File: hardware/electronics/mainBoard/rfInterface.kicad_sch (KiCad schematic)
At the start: 0 parts

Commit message: added rf interface sch
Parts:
- added AE1: TNC, symbol lib_sch:Antenna_Shield
- added AE3, AE4: SMA, symbol lib_sch:Antenna_Shield
- added C85, C86: 100nF, symbol lib_sch:C
- added C87: 9.1pF, symbol lib_sch:C
- added C88: 5.6pF, symbol lib_sch:C_horizontal
- added C89: 9.1pF, symbol lib_sch:C_horizontal
- added C90: 100pF, symbol lib_sch:C_horizontal
- added C91: 100pF, symbol lib_sch:C
- added J12, J13, J14, J15: CONMHF1-SMD-T, symbol lib_sch:Conn_Coaxial
- added L4: 15nH, symbol lib_sch:L
- added L5: 6.8nH, symbol lib_sch:L
- added R57: 750R, symbol lib_sch:R
- added R58: 267R, symbol lib_sch:R_horizontal
- added R59: 49R9, symbol lib_sch:R
- added U17: PMA2-162LNA+, symbol lib_sch:PMA2-162LNA+
- added U18: QCN-19D+, symbol lib_sch:QCN-19D+
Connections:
- new net: C88.2, R58.1
- new net AUX_RF-IN: AE3.1 (A), J15.1 (In)
- new net GNSS_CONN1: J12.1 (In), U18.4 (PORT1)
- new net GNSS_CONN2: J13.1 (In), U18.6 (PORT2)
- new net GNSS_RF-IN: AE1.1 (A), C89.1
- new net LNA_BIAS: R57.2, U17.4 (BIAS)
- new net LNA_FB: C88.1, U17.5 (FB)
- new net LNA_RBIAS: C85.1, C86.1, C87.1, L4.1, R57.1
- new net LNA_RF-GND: C91.1, L5.2, U17.3 (RF-GND)
- new net LNA_RF-IN: C89.2, L5.1, U17.2 (RF-IN)
- new net LNA_RF-OUT: C90.1, L4.2, R58.2, U17.7 (RF-OUT)
- new net LTE_RF-IN: AE4.1 (A), J14.1 (In)
- new net RF-SPLIT_50R: R59.1, U18.3 (50R)
- new net RF-SPLIT_SUM: C90.2, U18.1 (SUM)
- new net VSS: AE1.2 (Shield), AE3.2 (Shield), AE4.2 (Shield), C85.2, C86.2, C87.2, C91.2, J12.2 (Ext), J13.2 (Ext), J14.2 (Ext), J15.2 (Ext), R59.2, U17.1 (NC), U17.6 (NC), U17.8 (GND), U17.9 (GND), U18.2 (GND), U18.5 (GND)
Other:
- note added: "AUX Card Cable"
- note added: "GNSS Card Cable"
- note added: "LTE Card Cable"

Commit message: fixed power flags
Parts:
- AE3: now not fitted
- renumbered AE4 to AE2, C85 to C71, C86 to C72, C87 to C73, C88 to C74, C89 to C75, C90 to C76, C91 to C77, R57 to R48, R58 to R49, R59 to R50, U17 to U16, U18 to U17

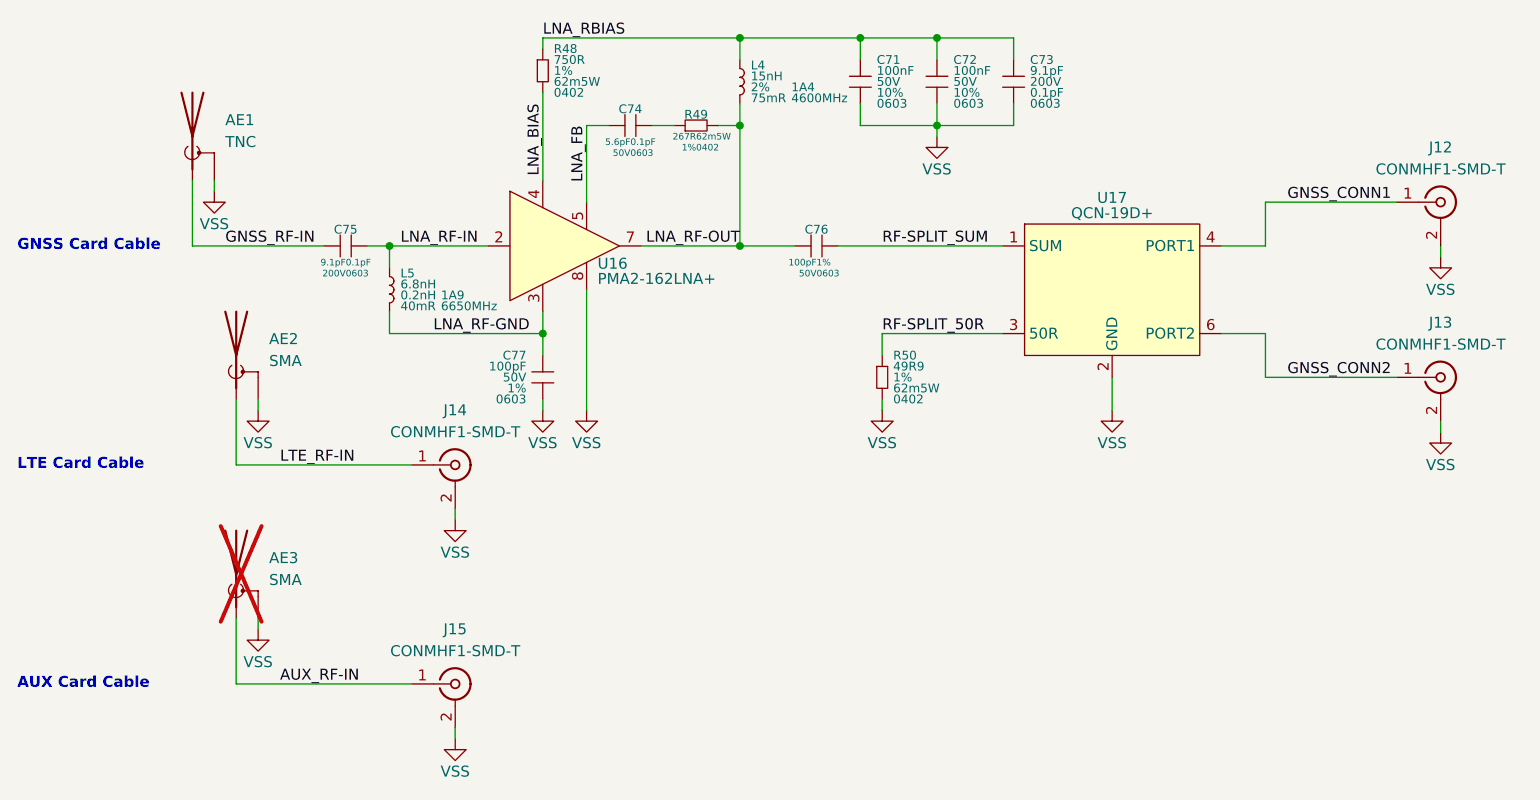
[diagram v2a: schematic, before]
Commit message: updated capacitors
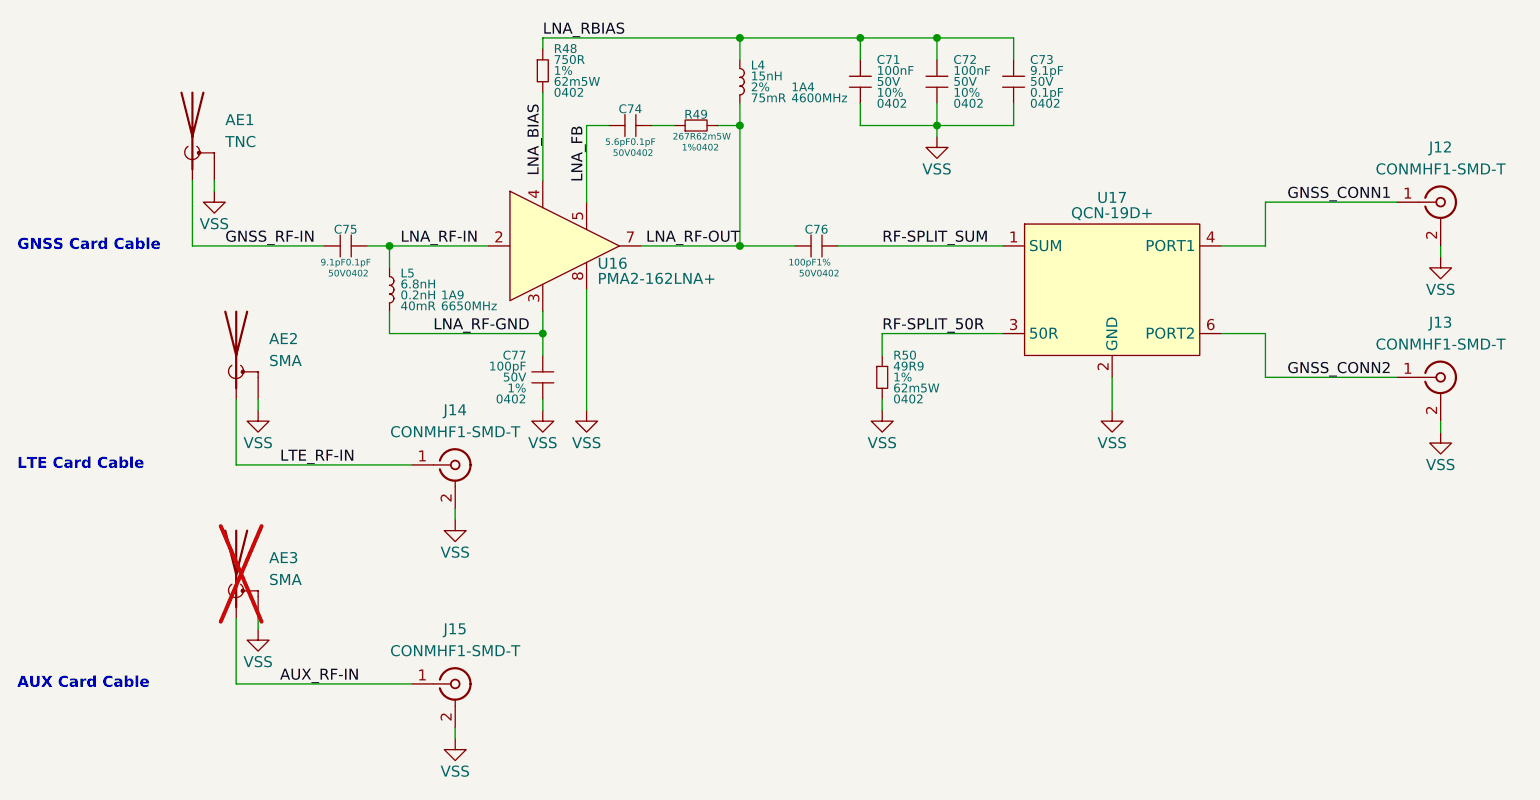
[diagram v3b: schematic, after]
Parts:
- C71, C72: DKPN 478-KAM15AR71H104KTCT-ND -> 490-GRT155R71H104KE01DCT-ND; MPN 06035C104K4T2A -> GRT155R71H104KE01D; Manufacturer KYOCERA AVX -> Murata Electronics; Package 0603 -> 0402
- C73, C75: DKPN 478-KGQ15ACG2D9R1BTCT-ND -> 490-GCM1555C1H9R1BA16DCT-ND; MPN KGQ15ACG2D9R1BT -> GCM1555C1H9R1BA16D; Manufacturer KYOCERA AVX -> Murata Electronics; Package 0603 -> 0402; Voltage Rating 200V -> 50V
- C74: DKPN 478-KGQ15ACG1H5R6BTCT-ND -> 490-14424-1-ND; MPN KGQ15ACG1H5R6BT -> GCM1555C1H5R6BA16D; Manufacturer KYOCERA AVX -> Murata Electronics; Package 0603 -> 0402
- C76, C77: DKPN 478-KGQ15ACG1H101FTCT-ND -> 490-14349-1-ND; MPN KGQ15ACG1H101FT -> GCM1555C1H101FA16D; Manufacturer KYOCERA AVX -> Murata Electronics; Package 0603 -> 0402

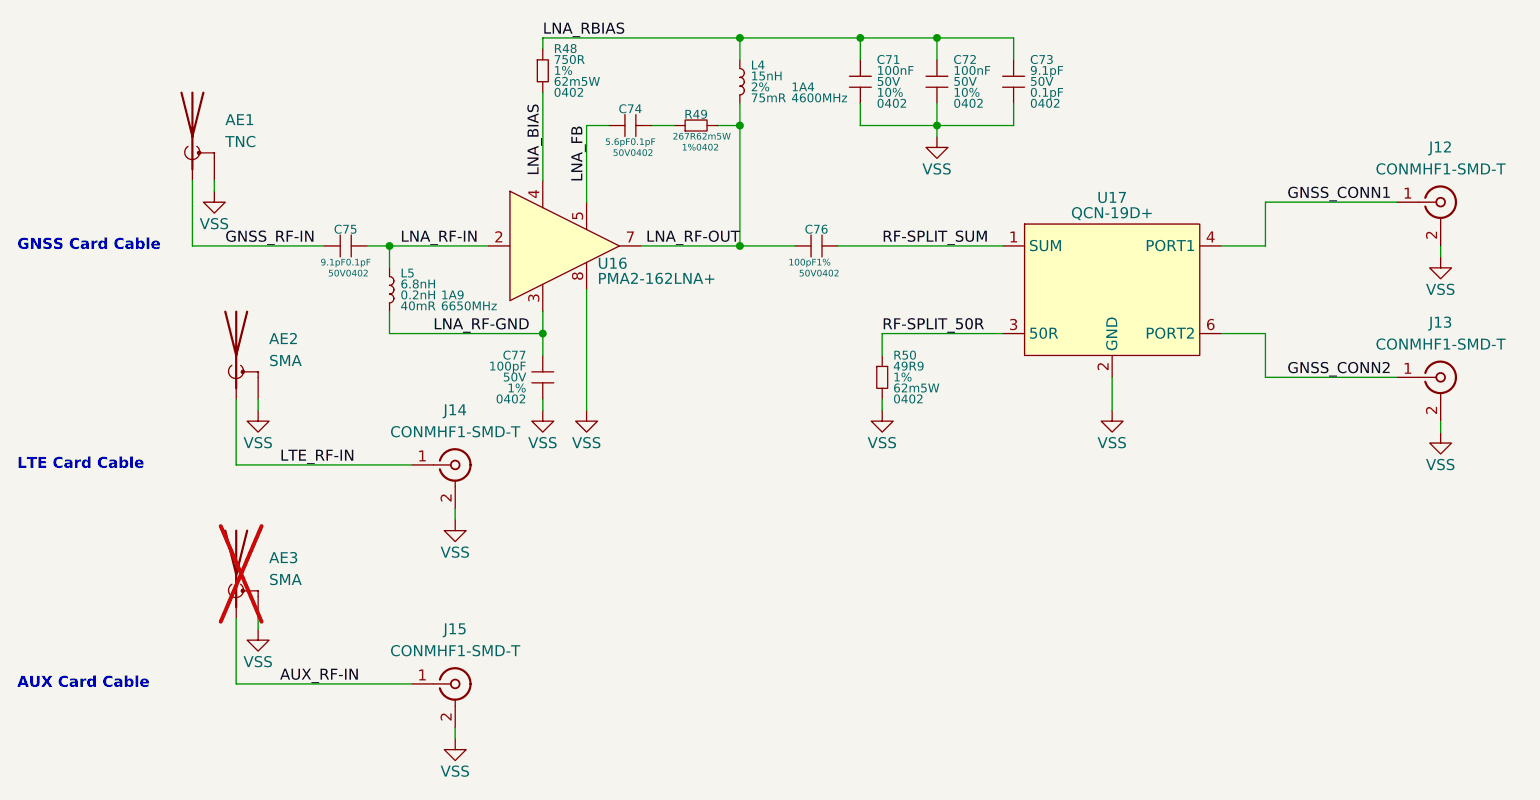
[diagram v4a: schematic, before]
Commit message: updated symbol refs
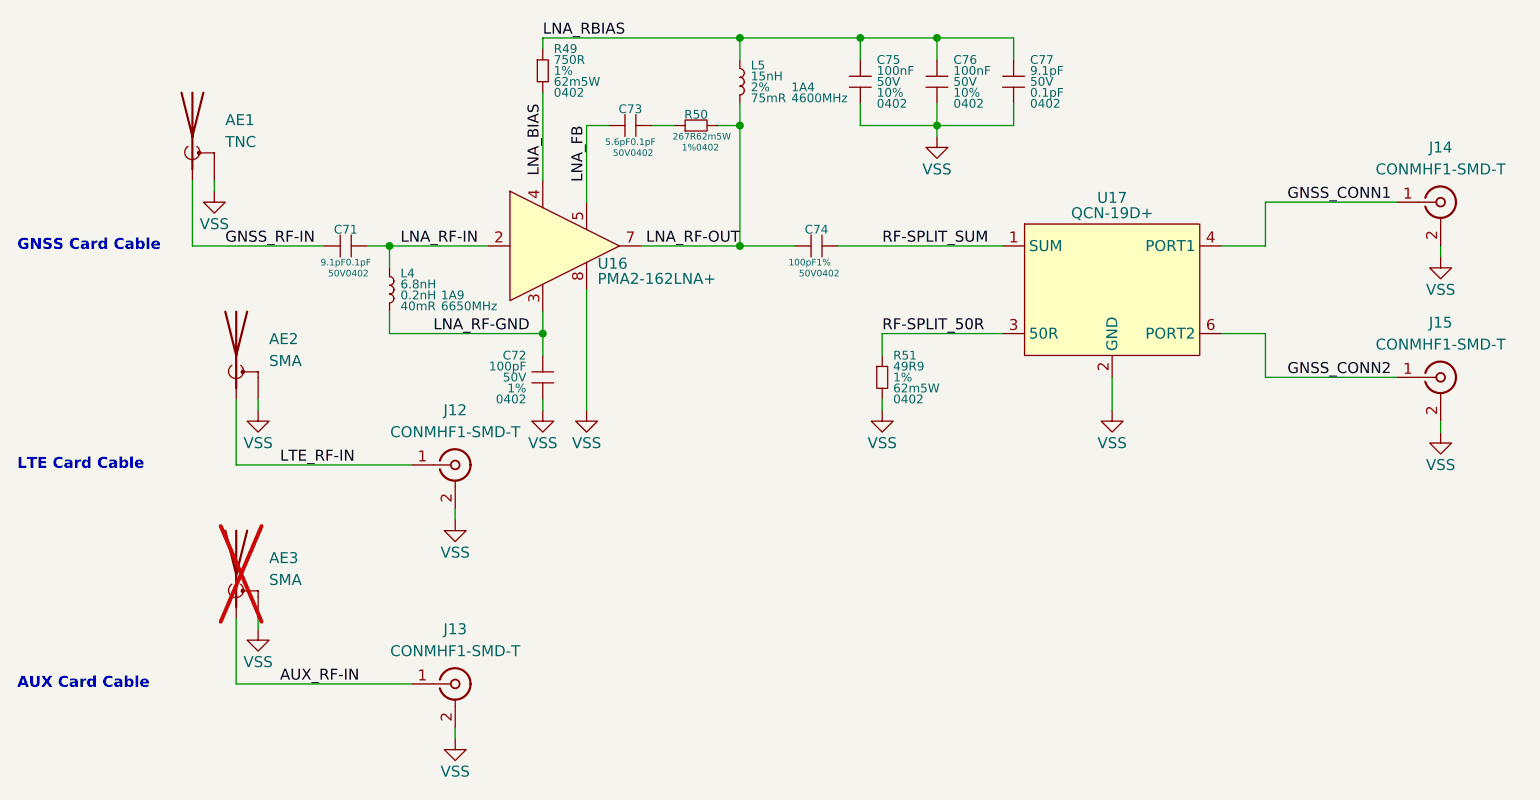
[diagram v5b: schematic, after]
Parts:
- renumbered C75 to C71, C77 to C72, C74 to C73, C76 to C74, C71 to C75, C72 to C76, C73 to C77, J14 to J12, J15 to J13, J12 to J14, J13 to J15, L5 to L4, L4 to L5, R48 to R49, R49 to R50, R50 to R51
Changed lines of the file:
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@@
 		(dnp no)
 		(fields_autoplaced yes)
-		(property "Reference" "#PWR0178"
+		(property "Reference" "#PWR0172"
 			(at 114.3 133.35 0)
 			(effects
@@
 			(project "mainBoard"
 				(path "/be16e32f-2ccf-4272-9ec7-94d5fe7a55e0/9566ea48-a930-4cf1-864c-3e42d00ab717"
-					(reference "#PWR0178")
+					(reference "#PWR0172")
 					(unit 1)
 				)
@@
 		(dnp no)
 		(fields_autoplaced yes)
-		(property "Reference" "C76"
+		(property "Reference" "C74"
 			(at 156.21 74.295 0)
 			(do_not_autoplace yes)
@@
 			(project "mainBoard"
 				(path "/be16e32f-2ccf-4272-9ec7-94d5fe7a55e0/9566ea48-a930-4cf1-864c-3e42d00ab717"
-					(reference "C76")
+					(reference "C74")
 					(unit 1)
 				)
@@
 		(dnp no)
 		(fields_autoplaced yes)
-		(property "Reference" "R49"
+		(property "Reference" "R50"
 			(at 142.24 60.96 0)
 			(do_not_autoplace yes)
@@
 			(project ""
 				(path "/be16e32f-2ccf-4272-9ec7-94d5fe7a55e0/9566ea48-a930-4cf1-864c-3e42d00ab717"
-					(reference "R49")
+					(reference "R50")
 					(unit 1)
 				)
@@
 		(dnp no)
 		(fields_autoplaced yes)
-		(property "Reference" "#PWR0175"
+		(property "Reference" "#PWR0179"
 			(at 228.6 97.79 0)
 			(effects
@@
 			(project "mainBoard"
 				(path "/be16e32f-2ccf-4272-9ec7-94d5fe7a55e0/9566ea48-a930-4cf1-864c-3e42d00ab717"
-					(reference "#PWR0175")
+					(reference "#PWR0179")
 					(unit 1)
 				)
@@
 		(dnp no)
 		(fields_autoplaced yes)
-		(property "Reference" "#PWR0176"
+		(property "Reference" "#PWR0171"
 			(at 114.3 107.95 0)
 			(effects
@@
 			(project "mainBoard"
 				(path "/be16e32f-2ccf-4272-9ec7-94d5fe7a55e0/9566ea48-a930-4cf1-864c-3e42d00ab717"
-					(reference "#PWR0176")
+					(reference "#PWR0171")
 					(unit 1)
 				)
@@
 		(on_board yes)
 		(dnp no)
-		(property "Reference" "L5"
+		(property "Reference" "L4"
 			(at 107.95 79.375 0)
 			(do_not_autoplace yes)
@@
 			(project ""
 				(path "/be16e32f-2ccf-4272-9ec7-94d5fe7a55e0/9566ea48-a930-4cf1-864c-3e42d00ab717"
-					(reference "L5")
+					(reference "L4")
 					(unit 1)
 				)
@@
 		(dnp no)
 		(fields_autoplaced yes)
-		(property "Reference" "#PWR0177"
+		(property "Reference" "#PWR0170"
 			(at 91.44 120.65 0)
 			(effects
@@
 			(project "mainBoard"
 				(path "/be16e32f-2ccf-4272-9ec7-94d5fe7a55e0/9566ea48-a930-4cf1-864c-3e42d00ab717"
-					(reference "#PWR0177")
+					(reference "#PWR0170")
 					(unit 1)
 				)
@@
 		(on_board yes)
 		(dnp no)
-		(property "Reference" "J15"
+		(property "Reference" "J13"
 			(at 114.3 120.65 0)
 			(effects
@@
 			(project "mainBoard"
 				(path "/be16e32f-2ccf-4272-9ec7-94d5fe7a55e0/9566ea48-a930-4cf1-864c-3e42d00ab717"
-					(reference "J15")
+					(reference "J13")
 					(unit 1)
 				)
@@
 		(on_board yes)
 		(dnp no)
-		(property "Reference" "J12"
+		(property "Reference" "J14"
 			(at 228.6 64.77 0)
 			(effects
@@
 			(project ""
 				(path "/be16e32f-2ccf-4272-9ec7-94d5fe7a55e0/9566ea48-a930-4cf1-864c-3e42d00ab717"
-					(reference "J12")
+					(reference "J14")
 					(unit 1)
 				)
@@
 		(dnp no)
 		(fields_autoplaced yes)
-		(property "Reference" "#PWR0170"
+		(property "Reference" "#PWR0169"
 			(at 91.44 95.25 0)
 			(effects
@@
 			(project "mainBoard"
 				(path "/be16e32f-2ccf-4272-9ec7-94d5fe7a55e0/9566ea48-a930-4cf1-864c-3e42d00ab717"
-					(reference "#PWR0170")
+					(reference "#PWR0169")
 					(unit 1)
 				)
@@
 		(dnp no)
 		(fields_autoplaced yes)
-		(property "Reference" "R48"
+		(property "Reference" "R49"
 			(at 125.73 53.34 0)
 			(do_not_autoplace yes)
@@
 			(project ""
 				(path "/be16e32f-2ccf-4272-9ec7-94d5fe7a55e0/9566ea48-a930-4cf1-864c-3e42d00ab717"
-					(reference "R48")
+					(reference "R49")
 					(unit 1)
 				)
@@
 		(dnp no)
 		(fields_autoplaced yes)
-		(property "Reference" "C71"
+		(property "Reference" "C75"
 			(at 163.195 54.61 0)
 			(do_not_autoplace yes)
@@
 			(project "mainBoard"
 				(path "/be16e32f-2ccf-4272-9ec7-94d5fe7a55e0/9566ea48-a930-4cf1-864c-3e42d00ab717"
-					(reference "C71")
+					(reference "C75")
 					(unit 1)
 				)
@@
 		(on_board yes)
 		(dnp no)
-		(property "Reference" "J13"
+		(property "Reference" "J15"
 			(at 228.6 85.09 0)
 			(effects
@@
 			(project "mainBoard"
 				(path "/be16e32f-2ccf-4272-9ec7-94d5fe7a55e0/9566ea48-a930-4cf1-864c-3e42d00ab717"
-					(reference "J13")
+					(reference "J15")
 					(unit 1)
 				)
@@
 		(on_board yes)
 		(dnp no)
-		(property "Reference" "L4"
+		(property "Reference" "L5"
 			(at 148.59 55.245 0)
 			(do_not_autoplace yes)
@@
 			(project "mainBoard"
 				(path "/be16e32f-2ccf-4272-9ec7-94d5fe7a55e0/9566ea48-a930-4cf1-864c-3e42d00ab717"
-					(reference "L4")
+					(reference "L5")
 					(unit 1)
 				)
@@
 		(dnp no)
 		(fields_autoplaced yes)
-		(property "Reference" "#PWR0173"
+		(property "Reference" "#PWR0175"
 			(at 163.83 95.25 0)
 			(effects
@@
 			(project "mainBoard"
 				(path "/be16e32f-2ccf-4272-9ec7-94d5fe7a55e0/9566ea48-a930-4cf1-864c-3e42d00ab717"
-					(reference "#PWR0173")
+					(reference "#PWR0175")
 					(unit 1)
 				)
@@
 		(dnp no)
 		(fields_autoplaced yes)
-		(property "Reference" "R50"
+		(property "Reference" "R51"
 			(at 165.1 88.9 0)
 			(do_not_autoplace yes)
@@
 			(project "mainBoard"
 				(path "/be16e32f-2ccf-4272-9ec7-94d5fe7a55e0/9566ea48-a930-4cf1-864c-3e42d00ab717"
-					(reference "R50")
+					(reference "R51")
 					(unit 1)
 				)
@@
 		(dnp no)
 		(fields_autoplaced yes)
-		(property "Reference" "#PWR0169"
+		(property "Reference" "#PWR0178"
 			(at 228.6 77.47 0)
 			(effects
@@
 			(project "mainBoard"
 				(path "/be16e32f-2ccf-4272-9ec7-94d5fe7a55e0/9566ea48-a930-4cf1-864c-3e42d00ab717"
-					(reference "#PWR0169")
+					(reference "#PWR0178")
 					(unit 1)
 				)
@@
 		(dnp no)
 		(fields_autoplaced yes)
-		(property "Reference" "#PWR0167"
+		(property "Reference" "#PWR0176"
 			(at 170.18 63.5 0)
 			(effects
@@
 			(project "mainBoard"
 				(path "/be16e32f-2ccf-4272-9ec7-94d5fe7a55e0/9566ea48-a930-4cf1-864c-3e42d00ab717"
-					(reference "#PWR0167")
+					(reference "#PWR0176")
 					(unit 1)
 				)
@@
 		(dnp no)
 		(fields_autoplaced yes)
-		(property "Reference" "C72"
+		(property "Reference" "C76"
 			(at 172.085 54.61 0)
 			(do_not_autoplace yes)
@@
 			(project "mainBoard"
 				(path "/be16e32f-2ccf-4272-9ec7-94d5fe7a55e0/9566ea48-a930-4cf1-864c-3e42d00ab717"
-					(reference "C72")
+					(reference "C76")
 					(unit 1)
 				)
@@
 		(dnp no)
 		(fields_autoplaced yes)
-		(property "Reference" "C74"
+		(property "Reference" "C73"
 			(at 134.62 60.325 0)
 			(do_not_autoplace yes)
@@
 			(project "mainBoard"
 				(path "/be16e32f-2ccf-4272-9ec7-94d5fe7a55e0/9566ea48-a930-4cf1-864c-3e42d00ab717"
-					(reference "C74")
+					(reference "C73")
 					(unit 1)
 				)
@@
 		(dnp no)
 		(fields_autoplaced yes)
-		(property "Reference" "#PWR0171"
+		(property "Reference" "#PWR0173"
 			(at 124.46 95.25 0)
 			(effects
@@
 			(project "mainBoard"
 				(path "/be16e32f-2ccf-4272-9ec7-94d5fe7a55e0/9566ea48-a930-4cf1-864c-3e42d00ab717"
-					(reference "#PWR0171")
+					(reference "#PWR0173")
 					(unit 1)
 				)
@@
 		(dnp no)
 		(fields_autoplaced yes)
-		(property "Reference" "#PWR0174"
+		(property "Reference" "#PWR0177"
 			(at 190.5 95.25 0)
 			(effects
@@
 			(project "mainBoard"
 				(path "/be16e32f-2ccf-4272-9ec7-94d5fe7a55e0/9566ea48-a930-4cf1-864c-3e42d00ab717"
-					(reference "#PWR0174")
+					(reference "#PWR0177")
 					(unit 1)
 				)
@@
 		(on_board yes)
 		(dnp no)
-		(property "Reference" "J14"
+		(property "Reference" "J12"
 			(at 114.3 95.25 0)
 			(effects
@@
 			(project "mainBoard"
 				(path "/be16e32f-2ccf-4272-9ec7-94d5fe7a55e0/9566ea48-a930-4cf1-864c-3e42d00ab717"
-					(reference "J14")
+					(reference "J12")
 					(unit 1)
 				)
@@
 		(dnp no)
 		(fields_autoplaced yes)
-		(property "Reference" "C75"
+		(property "Reference" "C71"
 			(at 101.6 74.295 0)
 			(do_not_autoplace yes)
@@
 			(project ""
 				(path "/be16e32f-2ccf-4272-9ec7-94d5fe7a55e0/9566ea48-a930-4cf1-864c-3e42d00ab717"
-					(reference "C75")
+					(reference "C71")
 					(unit 1)
 				)
@@
 		(dnp no)
 		(fields_autoplaced yes)
-		(property "Reference" "#PWR0172"
+		(property "Reference" "#PWR0174"
 			(at 129.54 95.25 0)
 			(effects
@@
 			(project "mainBoard"
 				(path "/be16e32f-2ccf-4272-9ec7-94d5fe7a55e0/9566ea48-a930-4cf1-864c-3e42d00ab717"
-					(reference "#PWR0172")
+					(reference "#PWR0174")
 					(unit 1)
 				)
@@
 		(on_board yes)
 		(dnp no)
-		(property "Reference" "C73"
+		(property "Reference" "C77"
 			(at 180.975 54.61 0)
 			(do_not_autoplace yes)
@@
 			(project "mainBoard"
 				(path "/be16e32f-2ccf-4272-9ec7-94d5fe7a55e0/9566ea48-a930-4cf1-864c-3e42d00ab717"
-					(reference "C73")
+					(reference "C77")
 					(unit 1)
 				)
@@
 		(on_board yes)
 		(dnp no)
-		(property "Reference" "C77"
+		(property "Reference" "C72"
 			(at 122.555 88.9 0)
 			(do_not_autoplace yes)
@@
 			(project ""
 				(path "/be16e32f-2ccf-4272-9ec7-94d5fe7a55e0/9566ea48-a930-4cf1-864c-3e42d00ab717"
-					(reference "C77")
+					(reference "C72")
 					(unit 1)
 				)
